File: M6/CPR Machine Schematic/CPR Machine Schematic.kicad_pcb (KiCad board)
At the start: 2 copper layers, 84.1 x 63 mm, 85 parts, among them J1 Battery 22.2V IN, J10 Laser Port, J11 Raspberry_Pi_2_3, J2 Power Switch, J3 GND Spare Headers, J4 +V Spare Headers, J5 Conn_02x20_Odd_Even, J6 I2C Port, J7 Stop Button Port, J8 Go Button Port, J9 Force Sensor, Q1 DMMT5401 PNP, Q2 SSM3J332R, Q3 DMG2305UX-EV, Q4 DMMT5401 PNP, Q5 T2N7002BK,LM, Q6 T2N7002BK,LM, Q7 T2N7002BK,LM, U1 3.3V Buck, U2 12V Buck, U3 MAX42403AFLB+, U4 MCP6004, U5 MCP3021A0T-E_OT

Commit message: More Revisions
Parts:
- J6: footprint Connector_PinHeader_2.54mm:PinHeader_1x02_P2.54mm_Vertical -> Connector_PinHeader_2.54mm:PinHeader_1x04_P2.54mm_Vertical
- U5: value MCP3021A0T-E_OT -> MCP3021A5T-E_OT
- moved J10 5.29 mm to (189.5, 77.5), turned to 180 degrees
- moved J9 4.25 mm to (189.0, 113.8)
- moved C11 3.20 mm to (189.4, 84.9)
- moved J8 3.20 mm to (185.1, 92.6)
- moved J7 3.17 mm to (185.2, 103.9)
- moved C10 3.17 mm to (189.4, 96.3)
- moved TP7 1.65 mm to (180.8, 126.4)
- moved TP8 1.65 mm to (180.8, 123.8)
- moved TP1 1.52 mm to (118.1, 87.9)
- moved J6 1.38 mm to (186.4, 126.7)
- moved TP2 1.27 mm to (118.1, 81.8)
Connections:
- J6 pad 1: /Raspi/I2C_SDA -> +3.3V
- J6 pad 2: /Raspi/I2C_SCL -> GND
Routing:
- net +3.3V: track 244.8 -> 264.5 mm
- net Net-(J10-Pin_1): track 12.5 -> 17.2 mm
- net Net-(J10-Pin_2): track 11.9 -> 8.17 mm
- net /HMI_Raspi/Go Button: track 69.4 -> 72.7 mm
- net /HMI_Raspi/Stop Button: track 66.4 -> 69.6 mm
- net /HMI_Raspi/Go Button Ground: track 12.5 -> 15.7 mm
- net Net-(J9-Pin_1): track 31.9 -> 28.9 mm
- net /HMI_Raspi/Stop LED Power: track 6.97 -> 9.94 mm
- net /HMI_Raspi/Stop Button Ground: track 12.4 -> 15.3 mm
- net /HMI_Raspi/Go LED Power: track 10.7 -> 12.7 mm
- net /Raspi/I2C_SDA: track 33.1 -> 31.4 mm, vias 2 -> 3
- net +12V: track 78.7 -> 79.4 mm
- net /HMI_Raspi/Laser_PWM: track 93.5 -> 92.9 mm
- net /Raspi/I2C_SCL: track 35.9 -> 35.6 mm, vias 3 -> 2

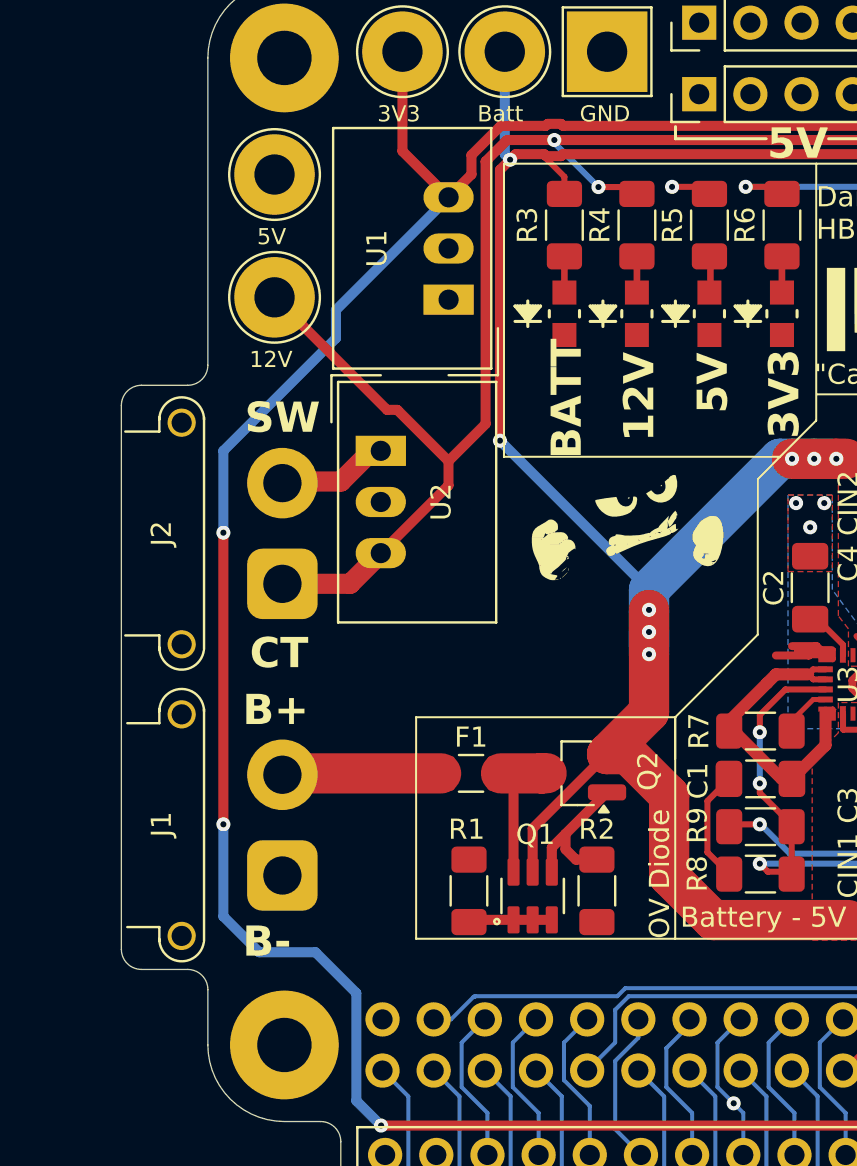
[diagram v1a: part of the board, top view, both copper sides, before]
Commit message: Reduced Xt30 interference w/ raspi IO
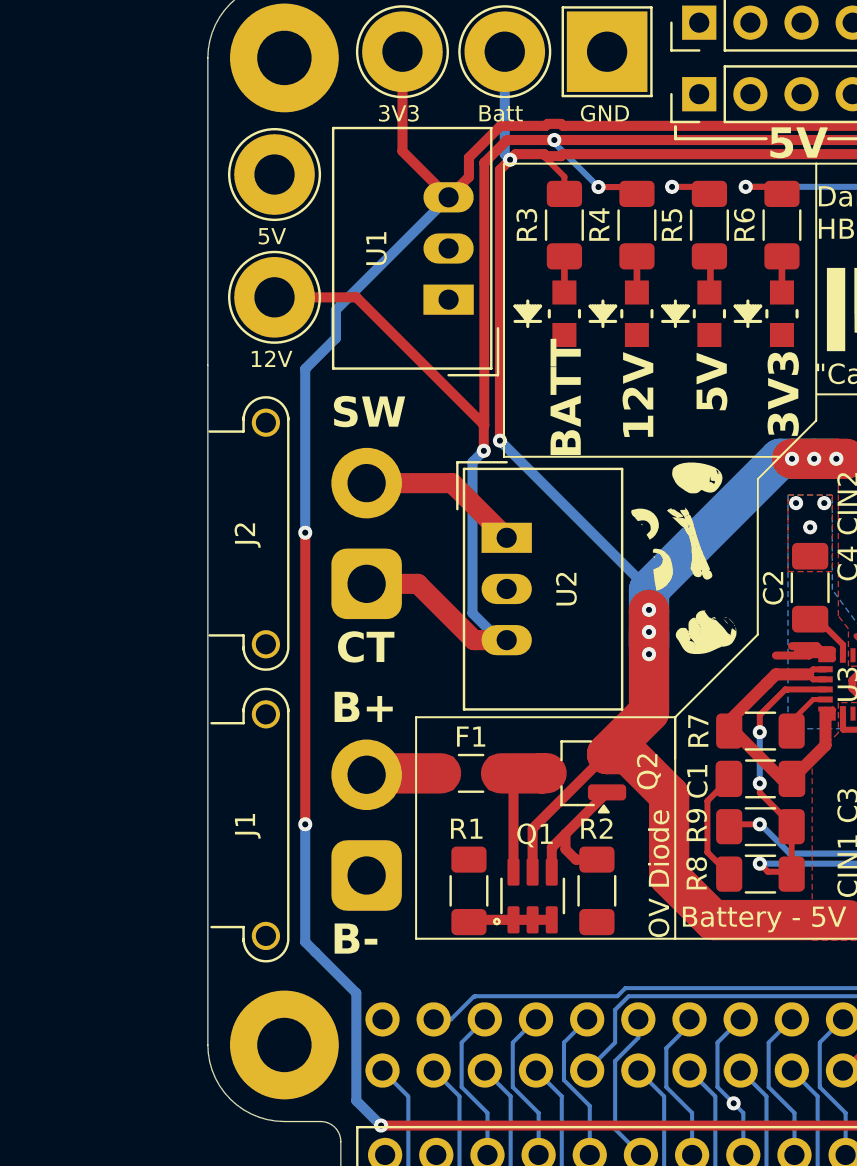
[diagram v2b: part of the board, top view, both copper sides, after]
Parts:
- moved U2 7.60 mm to (129.6, 99.8)
- moved J1 4.18 mm to (122.7, 116.6)
- moved J2 4.18 mm to (122.7, 102.1)
- moved REF**1 3.16 mm to (137.2, 100.8), turned to 90 degrees
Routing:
- net +12V: track 79.4 -> 86.3 mm, vias 2 -> 3
- net +3.3V: track 264.5 -> 259.5 mm
- net /Power/Battery +: track 7.91 -> 3.73 mm
- net /Power/From Switch: track 5.35 -> 8.08 mm
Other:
- board size 84.1 x 63 mm -> 79.8 x 63 mm

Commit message: Prod files for V3
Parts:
- moved G***2 9.88 mm to (162.1, 84.1)
- moved G***3 3.52 mm to (167.6, 87.6)
- moved G***1 0.65 mm to (149.6, 87.9)
- moved REF**2 0.49 mm to (158.5, 87.9)
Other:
- board text added: "{dblquote}You sound like Wario if he was Mexican{dblquote}"
- board text removed: "{dblquote}Can we get rid of Canada?{dblquote}"
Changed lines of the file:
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@@
 	(footprint "Images:MIT"
 		(layer "F.Cu")
-		(at 149.4 88.5)
+		(at 149.606 87.884)
 		(property "Reference" "G***1"
 			(at 0 0 0)
@@
 	(footprint "Images:LilGuy"
 		(layer "F.Cu")
-		(at 170.1 89.8)
+		(at 162.052 84.074)
 		(property "Reference" "G***2"
 			(at 0 0 0)
@@
 	(footprint "MAX42402AFLB_:Untitled"
 		(layer "F.Cu")
-		(at 158.75 88.3)
+		(at 158.496 87.884)
 		(property "Reference" "REF**2"
 			(at 0 -0.5 0)
@@
 	(footprint "Images:Occam"
 		(layer "F.Cu")
-		(at 165.3 85)
+		(at 167.64 87.63)
 		(property "Reference" "G***3"
 			(at 0 0 0)
@@
 	)
 	(gr_text "Daniel Gliksberg\nHB Main Board v3"
-		(at 145 85.1 0)
+		(at 145.288 84.582 0)
 		(layer "F.SilkS")
 		(effects
@@
 		)
 	)
-	(gr_text "{dblquote}Can we get rid of Canada?{dblquote}"
-		(at 144.9 92.3 0)
+	(gr_text "{dblquote}You sound like Wario if he was Mexican{dblquote}"
+		(at 145.288 92.3 0)
 		(layer "F.SilkS")
 		(effects
 			(font
-				(size 1 1)
+				(size 0.8 0.8)
 				(thickness 0.15)
 			)
